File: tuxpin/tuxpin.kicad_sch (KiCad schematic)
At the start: 23 parts, among them Q1 BC817, Q2 BC817, Q3 BC817, Q4 BC817, Q5 BC817, Q6 BC817, U1 PST-540, U2 MAX16054AZT

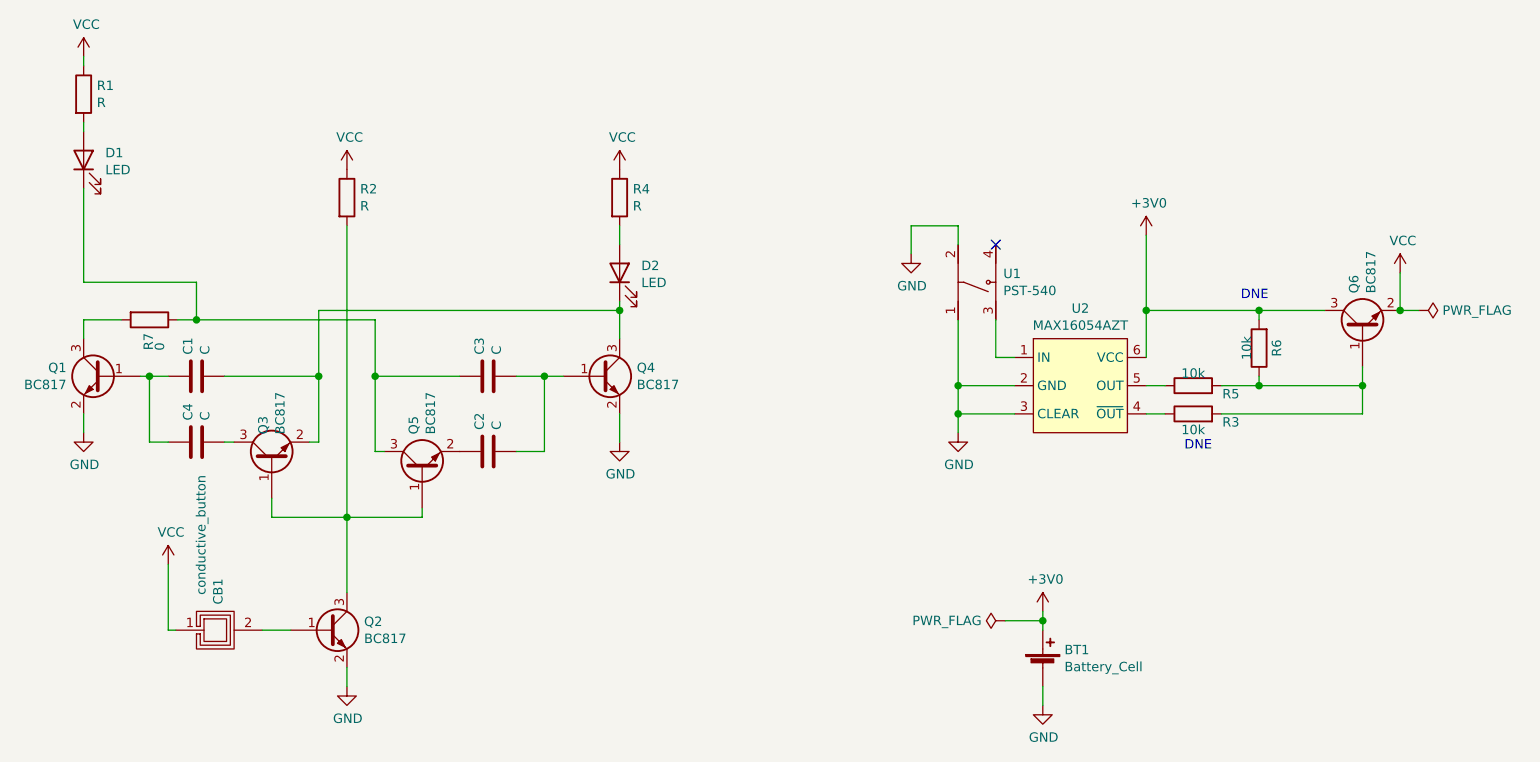
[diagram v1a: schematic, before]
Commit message: first version of pcb -> ERC doesn't pass
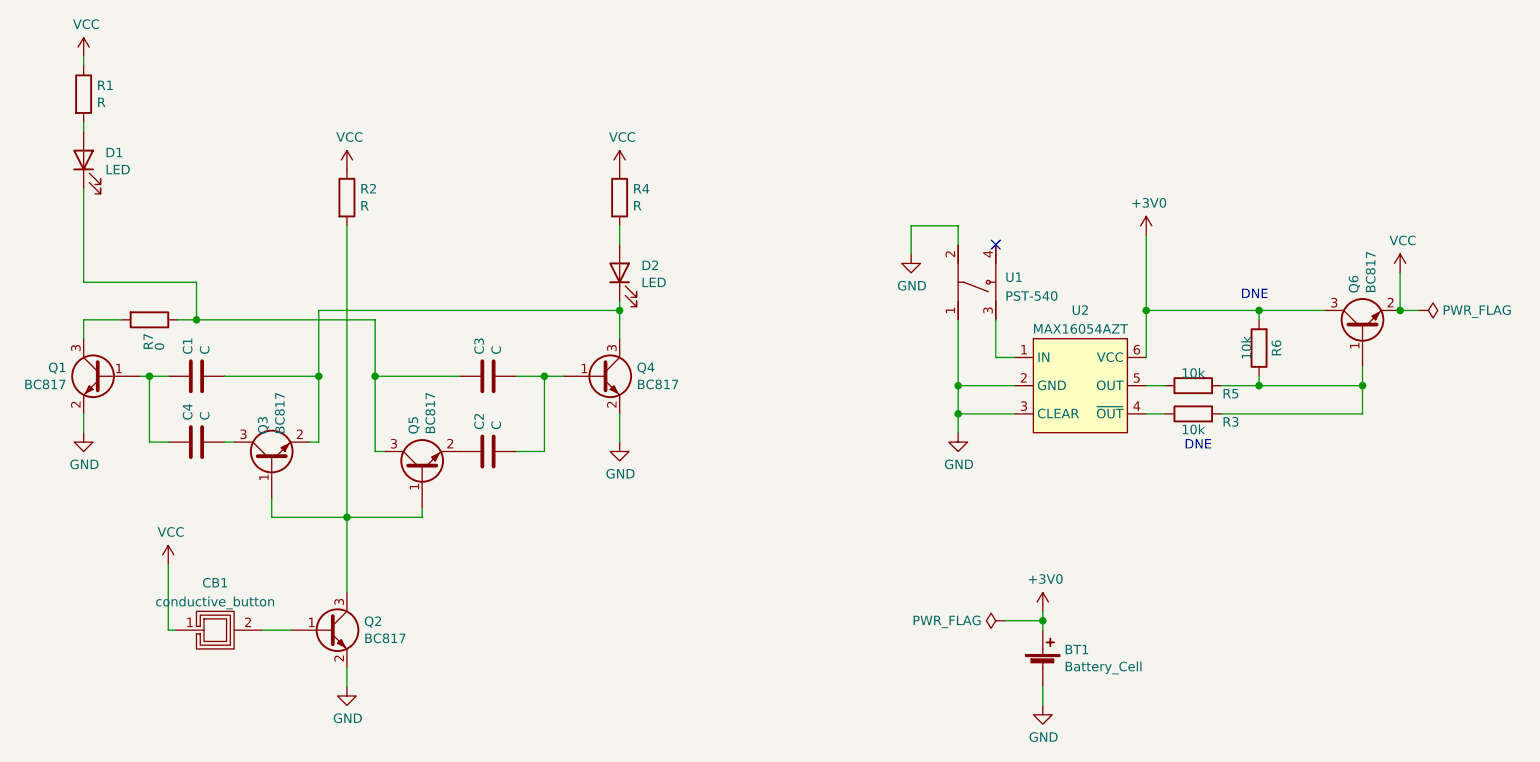
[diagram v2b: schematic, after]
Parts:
- removed CB1: conductive_button, dodo_button_and_switch:cat_back, symbol dodo-buttons:conductive_button
- removed U1: PST-540, dodo_button_and_switch:PTS-540, symbol dodo-buttons:PST-540
- removed U2: MAX16054AZT, Package_TO_SOT_SMD:SOT-23-6_Handsoldering, symbol dodo-device:MAX16054AZT
- added CB1: conductive_button, dodo_button_and_switch:cat_back, symbol dodo_buttons:conductive_button
- added U1: PST-540, dodo_button_and_switch:PTS-540, symbol dodo_buttons:PST-540
- added U2: MAX16054AZT, Package_TO_SOT_SMD:SOT-23-6_Handsoldering, symbol dodo_device:MAX16054AZT
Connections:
- net +3V0: now also U2.6 (VCC)
- net GND: now also U1.1, U1.2, U2.2 (GND), U2.3 (CLEAR)
- net VCC: now also CB1.1
- net at Q2.1 (B): now also CB1.2
- net at R5.1: now also U2.5 (OUT)
- net at R3.1: now also U2.4 (~{OUT})
- new net: U1.3, U2.1 (IN)

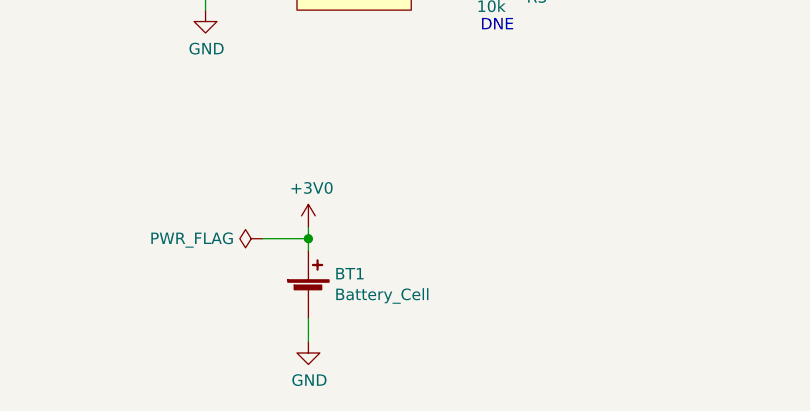
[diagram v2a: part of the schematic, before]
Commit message: drc almost without errors - library error battery holder
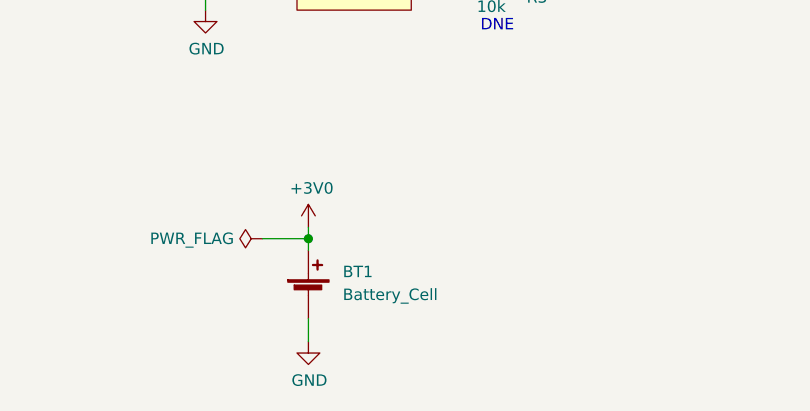
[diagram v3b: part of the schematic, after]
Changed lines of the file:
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@@
     (pin "1")
+  )
+  (symbol (lib_id "Device:Battery_Cell") (at 213.36 116.84 0) (unit 1)
+    (in_bom yes) (on_board yes) (fields_autoplaced)
+    (property "Reference" "BT1" (id 0) (at 217.17 114.173 0)
+      (effects (font (size 1.27 1.27)) (justify left))
+    )
+    (property "Value" "Battery_Cell" (id 1) (at 217.17 116.713 0)
+      (effects (font (size 1.27 1.27)) (justify left))
+    )
+    (property "Footprint" "Battery:BatteryHolder_Keystone_3000_1x12mm" (id 2) (at 213.36 115.316 90)
+      (effects (font (size 1.27 1.27)) hide)
+    )
+    (property "Datasheet" "~" (id 3) (at 213.36 115.316 90)
+      (effects (font (size 1.27 1.27)) hide)
+    )
+    (pin "1")
+    (pin "2")
   )
   (symbol (lib_id "Device:R") (at 92.71 69.85 270) (unit 1)
@@
     )
     (property "Datasheet" "~" (id 3) (at 92.71 69.85 0)
-      (effects (font (size 1.27 1.27)) hide)
-    )
-    (pin "1")
-    (pin "2")
-  )
-  (symbol (lib_id "Device:Battery_Cell") (at 213.36 116.84 0) (unit 1)
-    (in_bom yes) (on_board yes)
-    (property "Reference" "BT1" (id 0) (at 216.2811 114.4206 0)
-      (effects (font (size 1.27 1.27)) (justify left))
-    )
-    (property "Value" "Battery_Cell" (id 1) (at 216.2811 116.7193 0)
-      (effects (font (size 1.27 1.27)) (justify left))
-    )
-    (property "Footprint" "Battery:BatteryHolder_Keystone_3000_1x12mm" (id 2) (at 213.36 115.316 90)
-      (effects (font (size 1.27 1.27)) hide)
-    )
-    (property "Datasheet" "~" (id 3) (at 213.36 115.316 90)
       (effects (font (size 1.27 1.27)) hide)
     )
@@
       (reference "#PWR0113") (unit 1) (value "VCC") (footprint "")
     )
-    (path "/494aa4a8-1901-420c-a569-f0f529a58159"
+    (path "/429cf994-2b1e-44cf-af81-f4ee1363479a"
       (reference "BT1") (unit 1) (value "Battery_Cell") (footprint "Battery:BatteryHolder_Keystone_3000_1x12mm")
     )
